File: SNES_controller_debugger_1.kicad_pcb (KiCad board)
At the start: 2 copper layers, 100 x 74 mm, 21 parts, among them J1 ICSP, J2 CONTROLLER_OUT, J3 MICRO_USB, SW1 Reset_switch, U1 ATmega32U4, Y1 16MHz

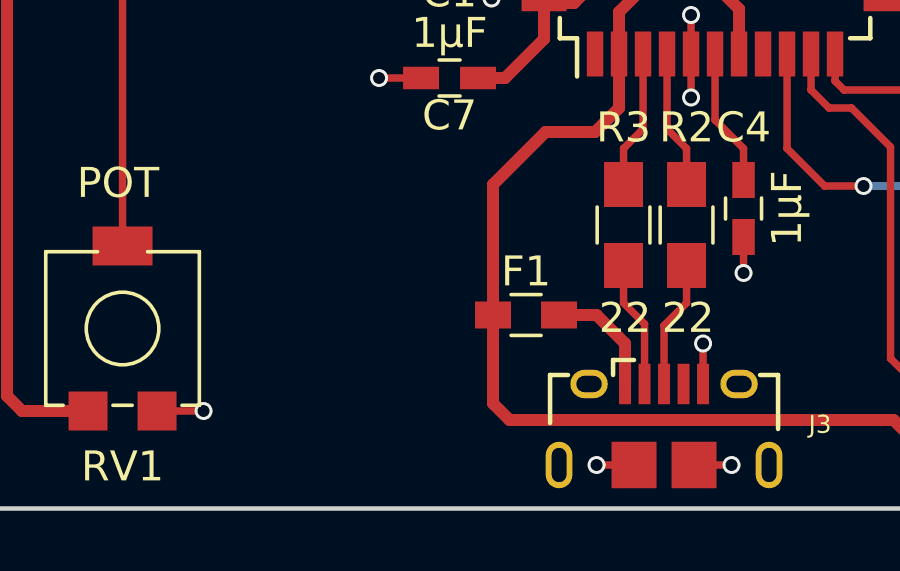
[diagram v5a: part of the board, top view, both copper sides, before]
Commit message: pcb: Add Digi-Key part numbers and MPNs to some components
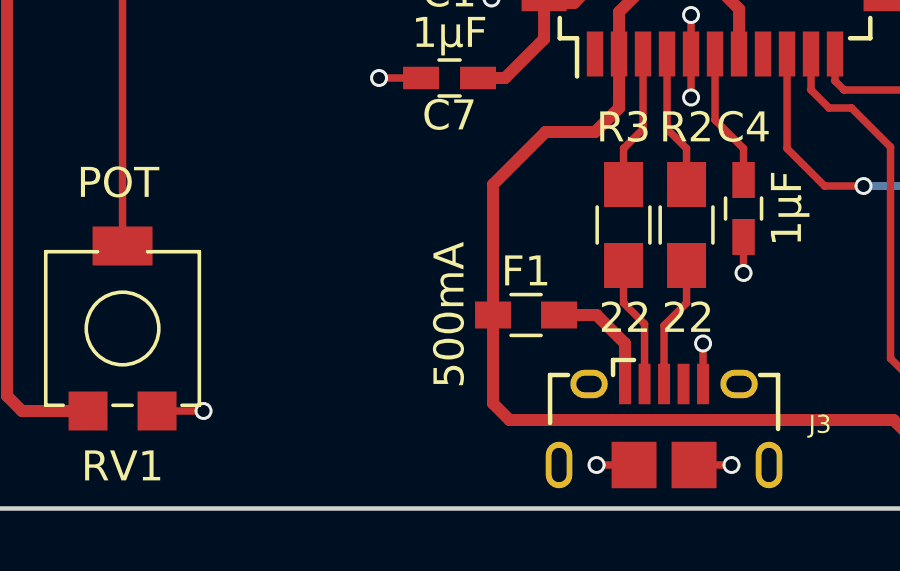
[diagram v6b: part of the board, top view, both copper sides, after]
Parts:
- D1, D2: value (none) -> MBR0520
- F1: value Polyfuse -> 500mA
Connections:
- DS1 pad 10: Net-(DS1-Pad10) -> (no net)
- DS1 pad 7: Net-(DS1-Pad7) -> (no net)
- DS1 pad 8: Net-(DS1-Pad8) -> (no net)
- DS1 pad 9: Net-(DS1-Pad9) -> (no net)
- J2 pad 5: Net-(J2-Pad5) -> (no net)
- J2 pad 6: Net-(J2-Pad6) -> (no net)
- J3 pad 4: Net-(J3-Pad4) -> (no net)
- U1 pad 1: Net-(U1-Pad1) -> (no net)
- U1 pad 12: Net-(U1-Pad12) -> (no net)
- U1 pad 18: Net-(U1-Pad18) -> (no net)
- U1 pad 19: Net-(U1-Pad19) -> (no net)
- U1 pad 20: Net-(U1-Pad20) -> (no net)
- U1 pad 21: Net-(U1-Pad21) -> (no net)
- U1 pad 22: Net-(U1-Pad22) -> (no net)
- U1 pad 30: Net-(U1-Pad30) -> (no net)
- U1 pad 39: Net-(U1-Pad39) -> (no net)
- U1 pad 40: Net-(U1-Pad40) -> (no net)
- U1 pad 41: Net-(U1-Pad41) -> (no net)
- U1 pad 8: Net-(U1-Pad8) -> (no net)
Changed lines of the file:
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@@
     (links 68)
     (no_connects 0)
-    (area 78.924999 86.924999 179.075001 161.075001)
+    (area 78.924999 86.924999 179.075001 162.575001)
     (thickness 0.8)
     (drawings 5)
@@
     (zones 0)
     (modules 21)
-    (nets 48)
+    (nets 29)
   )
   (page A4)
@@
   (net 27 IVCC)
   (net 28 "Net-(F1-Pad2)")
-  (net 29 "Net-(DS1-Pad7)")
-  (net 30 "Net-(DS1-Pad8)")
-  (net 31 "Net-(DS1-Pad9)")
-  (net 32 "Net-(DS1-Pad10)")
-  (net 33 "Net-(J2-Pad6)")
-  (net 34 "Net-(J2-Pad5)")
-  (net 35 "Net-(J3-Pad4)")
-  (net 36 "Net-(U1-Pad1)")
-  (net 37 "Net-(U1-Pad8)")
-  (net 38 "Net-(U1-Pad12)")
-  (net 39 "Net-(U1-Pad18)")
-  (net 40 "Net-(U1-Pad19)")
-  (net 41 "Net-(U1-Pad20)")
-  (net 42 "Net-(U1-Pad21)")
-  (net 43 "Net-(U1-Pad22)")
-  (net 44 "Net-(U1-Pad30)")
-  (net 45 "Net-(U1-Pad39)")
-  (net 46 "Net-(U1-Pad40)")
-  (net 47 "Net-(U1-Pad41)")
   (net_class Default "This is the default net class."
     (clearance 0.2)
@@
     (add_net "Net-(C3-Pad1)")
     (add_net "Net-(C4-Pad1)")
-    (add_net "Net-(DS1-Pad10)")
     (add_net "Net-(DS1-Pad3)")
-    (add_net "Net-(DS1-Pad7)")
-    (add_net "Net-(DS1-Pad8)")
-    (add_net "Net-(DS1-Pad9)")
-    (add_net "Net-(J2-Pad5)")
-    (add_net "Net-(J2-Pad6)")
     (add_net "Net-(J3-Pad2)")
     (add_net "Net-(J3-Pad3)")
-    (add_net "Net-(J3-Pad4)")
-    (add_net "Net-(U1-Pad1)")
-    (add_net "Net-(U1-Pad12)")
-    (add_net "Net-(U1-Pad18)")
-    (add_net "Net-(U1-Pad19)")
-    (add_net "Net-(U1-Pad20)")
-    (add_net "Net-(U1-Pad21)")
-    (add_net "Net-(U1-Pad22)")
-    (add_net "Net-(U1-Pad30)")
-    (add_net "Net-(U1-Pad39)")
-    (add_net "Net-(U1-Pad40)")
-    (add_net "Net-(U1-Pad41)")
-    (add_net "Net-(U1-Pad8)")
     (add_net RESET)
     (add_net SCLK)
@@
     (pad 6 thru_hole oval (at 0 12.7 90) (size 1.7 1.7) (drill 1) (layers *.Cu *.Mask)
       (net 10 LCD_E))
-    (pad 7 thru_hole oval (at 0 15.24 90) (size 1.7 1.7) (drill 1) (layers *.Cu *.Mask)
-      (net 29 "Net-(DS1-Pad7)"))
-    (pad 8 thru_hole oval (at 0 17.78 90) (size 1.7 1.7) (drill 1) (layers *.Cu *.Mask)
-      (net 30 "Net-(DS1-Pad8)"))
-    (pad 9 thru_hole oval (at 0 20.32 90) (size 1.7 1.7) (drill 1) (layers *.Cu *.Mask)
-      (net 31 "Net-(DS1-Pad9)"))
-    (pad 10 thru_hole oval (at 0 22.86 90) (size 1.7 1.7) (drill 1) (layers *.Cu *.Mask)
-      (net 32 "Net-(DS1-Pad10)"))
+    (pad 7 thru_hole oval (at 0 15.24 90) (size 1.7 1.7) (drill 1) (layers *.Cu *.Mask))
+    (pad 8 thru_hole oval (at 0 17.78 90) (size 1.7 1.7) (drill 1) (layers *.Cu *.Mask))
+    (pad 9 thru_hole oval (at 0 20.32 90) (size 1.7 1.7) (drill 1) (layers *.Cu *.Mask))
+    (pad 10 thru_hole oval (at 0 22.86 90) (size 1.7 1.7) (drill 1) (layers *.Cu *.Mask))
     (pad 11 thru_hole oval (at 0 25.4 90) (size 1.7 1.7) (drill 1) (layers *.Cu *.Mask)
       (net 11 LCD_D4))
@@
     (fp_line (start 5.175 -5.175) (end 4.5 -5.175) (layer F.SilkS) (width 0.15))
     (fp_line (start -5.175 -4.6) (end -6.45 -4.6) (layer F.SilkS) (width 0.15))
-    (pad 1 smd rect (at -5.7 -4 90) (size 1.5 0.55) (layers F.Cu F.Paste F.Mask)
-      (net 36 "Net-(U1-Pad1)"))
+    (pad 1 smd rect (at -5.7 -4 90) (size 1.5 0.55) (layers F.Cu F.Paste F.Mask))
     (pad 2 smd rect (at -5.7 -3.2 90) (size 1.5 0.55) (layers F.Cu F.Paste F.Mask)
       (net 6 UVCC))
@@
     (pad 7 smd rect (at -5.7 0.8 90) (size 1.5 0.55) (layers F.Cu F.Paste F.Mask)
       (net 6 UVCC))
-    (pad 8 smd rect (at -5.7 1.6 90) (size 1.5 0.55) (layers F.Cu F.Paste F.Mask)
-      (net 37 "Net-(U1-Pad8)"))
+    (pad 8 smd rect (at -5.7 1.6 90) (size 1.5 0.55) (layers F.Cu F.Paste F.Mask))
     (pad 9 smd rect (at -5.7 2.4 90) (size 1.5 0.55) (layers F.Cu F.Paste F.Mask)
       (net 16 SCLK))
@@
     (pad 11 smd rect (at -5.7 4 90) (size 1.5 0.55) (layers F.Cu F.Paste F.Mask)
       (net 15 MISO))
-    (pad 12 smd rect (at -4 5.7 180) (size 1.5 0.55) (layers F.Cu F.Paste F.Mask)
-      (net 38 "Net-(U1-Pad12)"))
+    (pad 12 smd rect (at -4 5.7 180) (size 1.5 0.55) (layers F.Cu F.Paste F.Mask))
     (pad 13 smd rect (at -3.2 5.7 180) (size 1.5 0.55) (layers F.Cu F.Paste F.Mask)
       (net 18 RESET))
@@
     (pad 17 smd rect (at 0 5.7 180) (size 1.5 0.55) (layers F.Cu F.Paste F.Mask)
       (net 4 "Net-(C3-Pad1)"))
-    (pad 18 smd rect (at 0.8 5.7 180) (size 1.5 0.55) (layers F.Cu F.Paste F.Mask)
-      (net 39 "Net-(U1-Pad18)"))
-    (pad 19 smd rect (at 1.6 5.7 180) (size 1.5 0.55) (layers F.Cu F.Paste F.Mask)
-      (net 40 "Net-(U1-Pad19)"))
-    (pad 20 smd rect (at 2.4 5.7 180) (size 1.5 0.55) (layers F.Cu F.Paste F.Mask)
-      (net 41 "Net-(U1-Pad20)"))
-    (pad 21 smd rect (at 3.2 5.7 180) (size 1.5 0.55) (layers F.Cu F.Paste F.Mask)
-      (net 42 "Net-(U1-Pad21)"))
-    (pad 22 smd rect (at 4 5.7 180) (size 1.5 0.55) (layers F.Cu F.Paste F.Mask)
-      (net 43 "Net-(U1-Pad22)"))
+    (pad 18 smd rect (at 0.8 5.7 180) (size 1.5 0.55) (layers F.Cu F.Paste F.Mask))
+    (pad 19 smd rect (at 1.6 5.7 180) (size 1.5 0.55) (layers F.Cu F.Paste F.Mask))
+    (pad 20 smd rect (at 2.4 5.7 180) (size 1.5 0.55) (layers F.Cu F.Paste F.Mask))
+    (pad 21 smd rect (at 3.2 5.7 180) (size 1.5 0.55) (layers F.Cu F.Paste F.Mask))
+    (pad 22 smd rect (at 4 5.7 180) (size 1.5 0.55) (layers F.Cu F.Paste F.Mask))
     (pad 23 smd rect (at 5.7 4 90) (size 1.5 0.55) (layers F.Cu F.Paste F.Mask)
       (net 2 Earth))
@@
     (pad 29 smd rect (at 5.7 -0.8 90) (size 1.5 0.55) (layers F.Cu F.Paste F.Mask)
       (net 20 LATCH_OUT))
-    (pad 30 smd rect (at 5.7 -1.6 90) (size 1.5 0.55) (layers F.Cu F.Paste F.Mask)
-      (net 44 "Net-(U1-Pad30)"))
+    (pad 30 smd rect (at 5.7 -1.6 90) (size 1.5 0.55) (layers F.Cu F.Paste F.Mask))
     (pad 31 smd rect (at 5.7 -2.4 90) (size 1.5 0.55) (layers F.Cu F.Paste F.Mask)
       (net 21 CLK_OUT))
@@
     (pad 38 smd rect (at 0.8 -5.7 180) (size 1.5 0.55) (layers F.Cu F.Paste F.Mask)
       (net 8 LCD_RS))
-    (pad 39 smd rect (at 0 -5.7 180) (size 1.5 0.55) (layers F.Cu F.Paste F.Mask)
-      (net 45 "Net-(U1-Pad39)"))
-    (pad 40 smd rect (at -0.8 -5.7 180) (size 1.5 0.55) (layers F.Cu F.Paste F.Mask)
-      (net 46 "Net-(U1-Pad40)"))
-    (pad 41 smd rect (at -1.6 -5.7 180) (size 1.5 0.55) (layers F.Cu F.Paste F.Mask)
-      (net 47 "Net-(U1-Pad41)"))
+    (pad 39 smd rect (at 0 -5.7 180) (size 1.5 0.55) (layers F.Cu F.Paste F.Mask))
+    (pad 40 smd rect (at -0.8 -5.7 180) (size 1.5 0.55) (layers F.Cu F.Paste F.Mask))
+    (pad 41 smd rect (at -1.6 -5.7 180) (size 1.5 0.55) (layers F.Cu F.Paste F.Mask))
     (pad 42 smd rect (at -2.4 -5.7 180) (size 1.5 0.55) (layers F.Cu F.Paste F.Mask)
       (net 1 "Net-(C1-Pad1)"))
@@
     (pad 3 smd rect (at 0 -2.7) (size 0.4 1.35) (layers F.Cu F.Paste F.Mask)
       (net 23 "Net-(J3-Pad3)"))
-    (pad 4 smd rect (at 0.65 -2.7) (size 0.4 1.35) (layers F.Cu F.Paste F.Mask)
-      (net 35 "Net-(J3-Pad4)"))
+    (pad 4 smd rect (at 0.65 -2.7) (size 0.4 1.35) (layers F.Cu F.Paste F.Mask))
     (pad 5 smd rect (at 1.3 -2.7) (size 0.4 1.35) (layers F.Cu F.Paste F.Mask)
       (net 2 Earth))
@@
     (pad 2 thru_hole circle (at 0 4 90) (size 2.2 2.2) (drill 1.3) (layers *.Cu *.Mask)
       (net 21 CLK_OUT))
-    (pad 6 thru_hole circle (at 0 22.5 90) (size 2.2 2.2) (drill 1.3) (layers *.Cu *.Mask)
-      (net 33 "Net-(J2-Pad6)"))
-    (pad 5 thru_hole circle (at 0 18.5 90) (size 2.2 2.2) (drill 1.3) (layers *.Cu *.Mask)
-      (net 34 "Net-(J2-Pad5)"))
+    (pad 6 thru_hole circle (at 0 22.5 90) (size 2.2 2.2) (drill 1.3) (layers *.Cu *.Mask))
+    (pad 5 thru_hole circle (at 0 18.5 90) (size 2.2 2.2) (drill 1.3) (layers *.Cu *.Mask))
     (pad 1 thru_hole rect (at 0 0 90) (size 2.2 2.2) (drill 1.3) (layers *.Cu *.Mask)
       (net 26 VCC))
@@
       (effects (font (size 1 1) (thickness 0.15)))
     )
-    (fp_text value "" (at 0 2.1 270) (layer F.Fab) hide
+    (fp_text value MBR0520 (at 0 2.1 270) (layer F.Fab) hide
       (effects (font (size 1 1) (thickness 0.15)))
     )
@@
       (effects (font (size 1 1) (thickness 0.15)))
     )
-    (fp_text value "" (at 0 2.1 180) (layer F.Fab) hide
+    (fp_text value MBR0520 (at 0 2.1 180) (layer F.Fab) hide
       (effects (font (size 1 1) (thickness 0.15)))
     )
@@
       (effects (font (size 1 1) (thickness 0.15)))
     )
-    (fp_text value Polyfuse (at 0 1.55) (layer F.Fab)
-      (effects (font (size 1 1) (thickness 0.15)))
-    )
+    (fp_text value 500mA (at -2.55 0 90) (layer F.SilkS)
+      (effects (font (size 1 1) (thickness 0.15)))
+    )

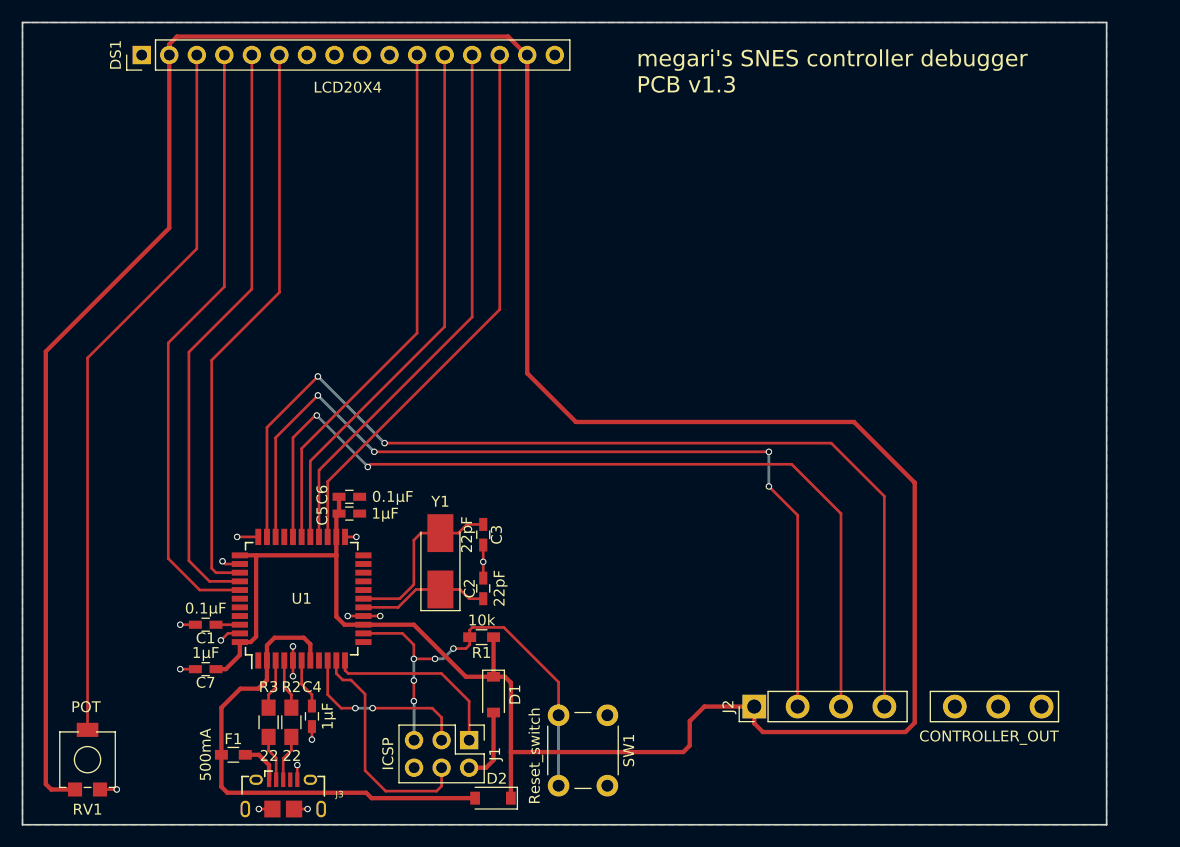
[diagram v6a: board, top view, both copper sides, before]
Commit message: pcb: Add hardware capability to dim the LCD backlight and to switch power to the LCD
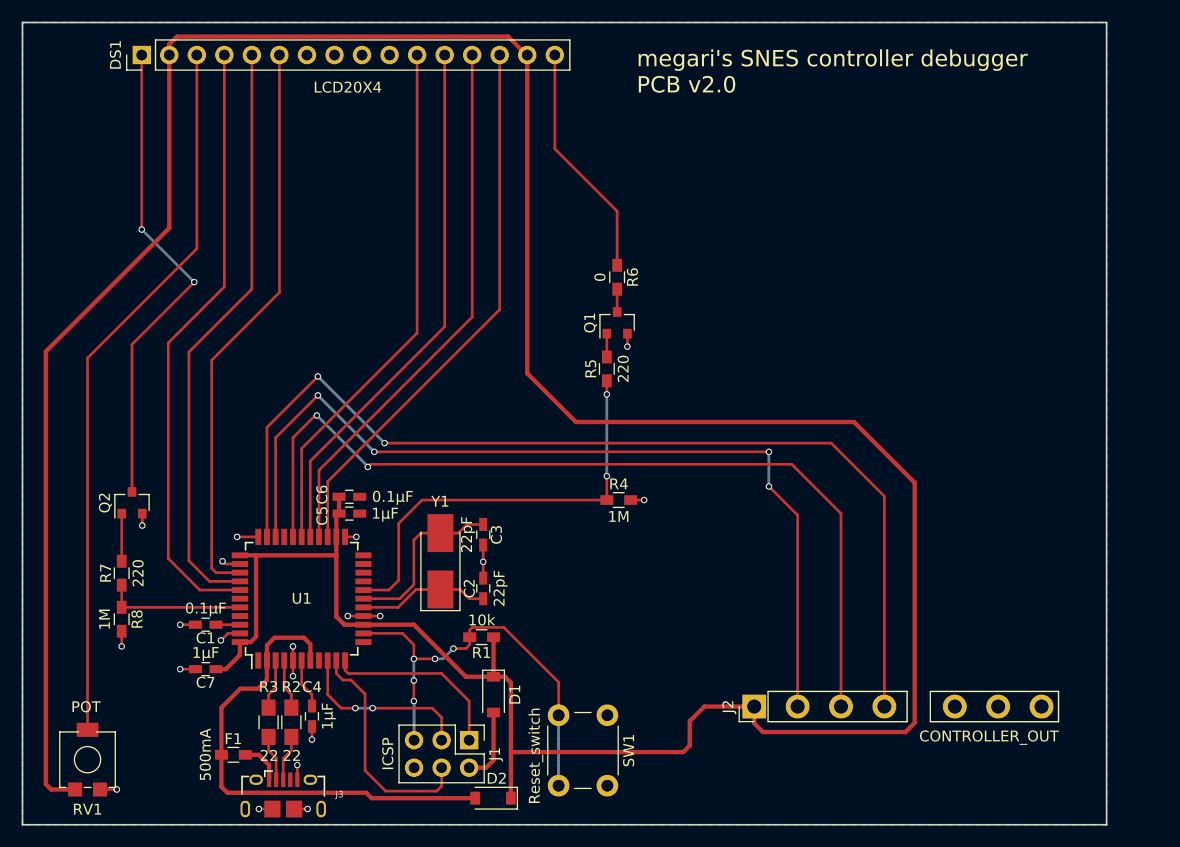
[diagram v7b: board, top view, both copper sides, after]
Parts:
- added Q1: DMG2302UK-7, TO_SOT_Packages_SMD:SOT-23, F.Cu at (133.8, 114.7)
- added Q2: DMG2302UK-7, TO_SOT_Packages_SMD:SOT-23, F.Cu at (89.1, 131.3)
- added R4: 1M, Resistors_SMD:R_0603_HandSoldering, F.Cu at (134.0, 131.1)
- added R5: 220, Resistors_SMD:R_0603_HandSoldering, F.Cu at (132.9, 119.0)
- added R6: 0, Resistors_SMD:R_0603_HandSoldering, F.Cu at (133.8, 110.5)
- added R7: 220, Resistors_SMD:R_0603_HandSoldering, F.Cu at (88.2, 137.8)
- added R8: 1M, Resistors_SMD:R_0603_HandSoldering, F.Cu at (88.2, 142.1)
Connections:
- DS1 pad 1: Earth -> Net-(DS1-Pad1)
- DS1 pad 16: Earth -> Net-(DS1-Pad16)
- U1 pad 18: (no net) -> LCD_LED
- U1 pad 40: (no net) -> LCD_PWR
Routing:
- net Net-(DS1-Pad1): track 0.00 -> 44.7 mm, vias 0 -> 2
- net LCD_LED: track 0.00 -> 40.0 mm, vias 0 -> 2
- net Net-(DS1-Pad16): track 0.00 -> 21.8 mm
- net LCD_PWR: track 0.00 -> 12.9 mm
- net Earth: track 24.9 -> 29.9 mm, vias 16 -> 20
- net Net-(Q2-Pad1): track 0.00 -> 4.40 mm
- net Net-(Q1-Pad1): track 0.00 -> 2.15 mm
- net Net-(Q1-Pad3): track 0.00 -> 2.10 mm
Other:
- board text added: "megari's SNES controller debugger PCB v2.0"
- board text removed: "megari's SNES controller debugger PCB v1.3"

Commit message: pcb, firmware: Using an N-MOSFET to cut power to the LCD from the negative side won't work, so use a P-MOSFET on the positive side
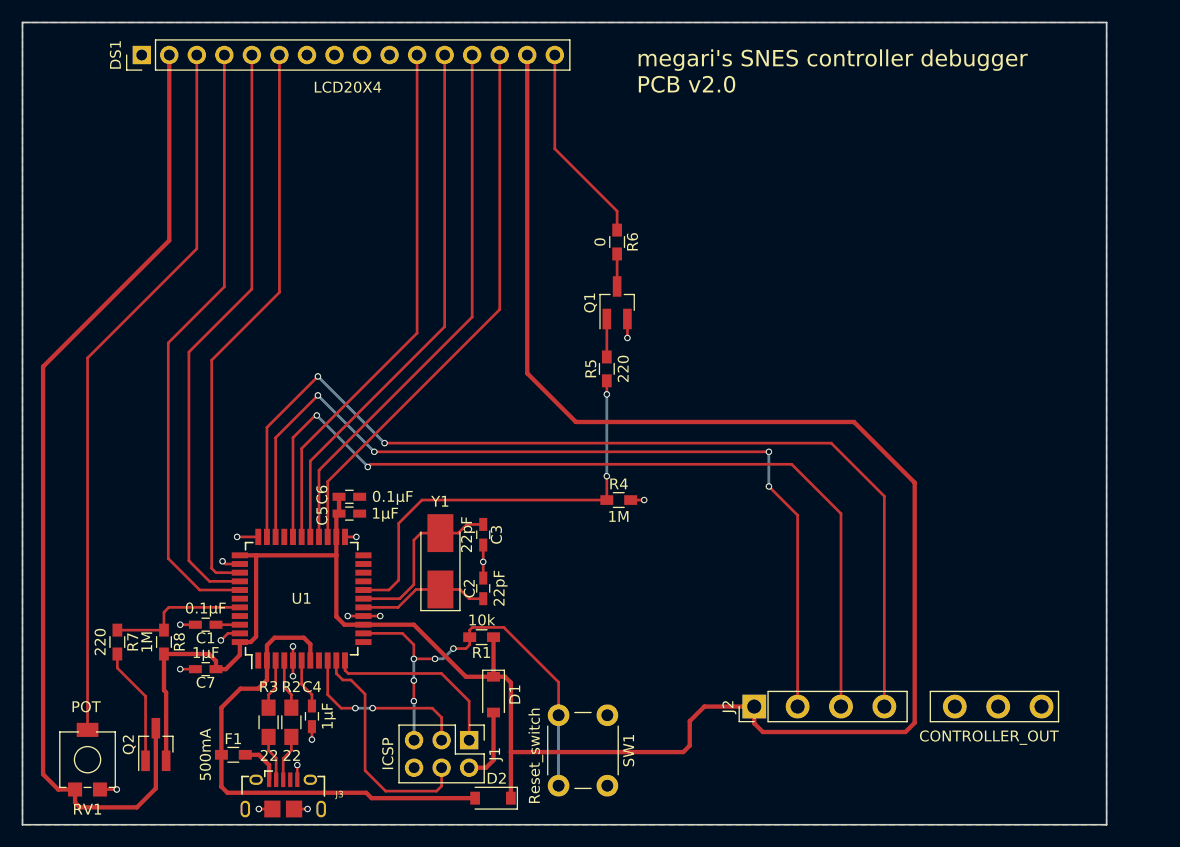
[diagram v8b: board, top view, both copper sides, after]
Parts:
- Q1: footprint TO_SOT_Packages_SMD:SOT-23 -> TO_SOT_Packages_SMD:SOT-23_Handsoldering
- Q2: value DMG2302UK-7 -> DMP2215L-7; footprint TO_SOT_Packages_SMD:SOT-23 -> TO_SOT_Packages_SMD:SOT-23_Handsoldering
- moved Q2 22.4 mm to (91.3, 153.6)
- moved R7 6.36 mm to (87.8, 144.2), turned to 270 degrees
- moved R8 4.43 mm to (92.0, 144.2)
- moved R6 3.25 mm to (133.8, 107.2)
- moved Q1 1.85 mm to (133.8, 112.8)
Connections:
- DS1 pad 1: Net-(DS1-Pad1) -> Earth
- DS1 pad 2: VCC -> Net-(DS1-Pad2)
- Q2 pad 2: Earth -> VCC
- Q2 pad 3: Net-(DS1-Pad1) -> Net-(DS1-Pad2)
- R8 pad 2: Earth -> VCC
- RV1 pad 3: VCC -> Net-(DS1-Pad2)
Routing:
- net VCC: track 311.0 -> 215.9 mm
- net Net-(DS1-Pad2): track 0.00 -> 89.8 mm
- net Net-(DS1-Pad1): track 44.7 -> 0.00 mm, vias 2 -> 0
- net Net-(Q2-Pad1): track 4.40 -> 10.9 mm
- net Net-(DS1-Pad16): track 21.8 -> 18.5 mm
- net Earth: track 29.9 -> 27.9 mm, vias 20 -> 18
- net Net-(Q1-Pad1): track 2.15 -> 4.00 mm
- net Net-(Q1-Pad3): track 2.10 -> 3.50 mm
